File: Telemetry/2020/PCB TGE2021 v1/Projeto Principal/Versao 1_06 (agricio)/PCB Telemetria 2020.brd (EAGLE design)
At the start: 160 x 100 mm, 57 parts, among them IC1 INA240A1DR, IC2 MCP3221A6T-E_OTVAO, IC3 AZ1117IH-3.3TRG1, IC4 ACS758LCB-050B-PFF-T, IC5 ADS1115IDGSR, IC6 ACS712-030B3, IC7 THVD2410DR, J1 172042-0406, J2 39-28-9048, J3 39-28-9048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

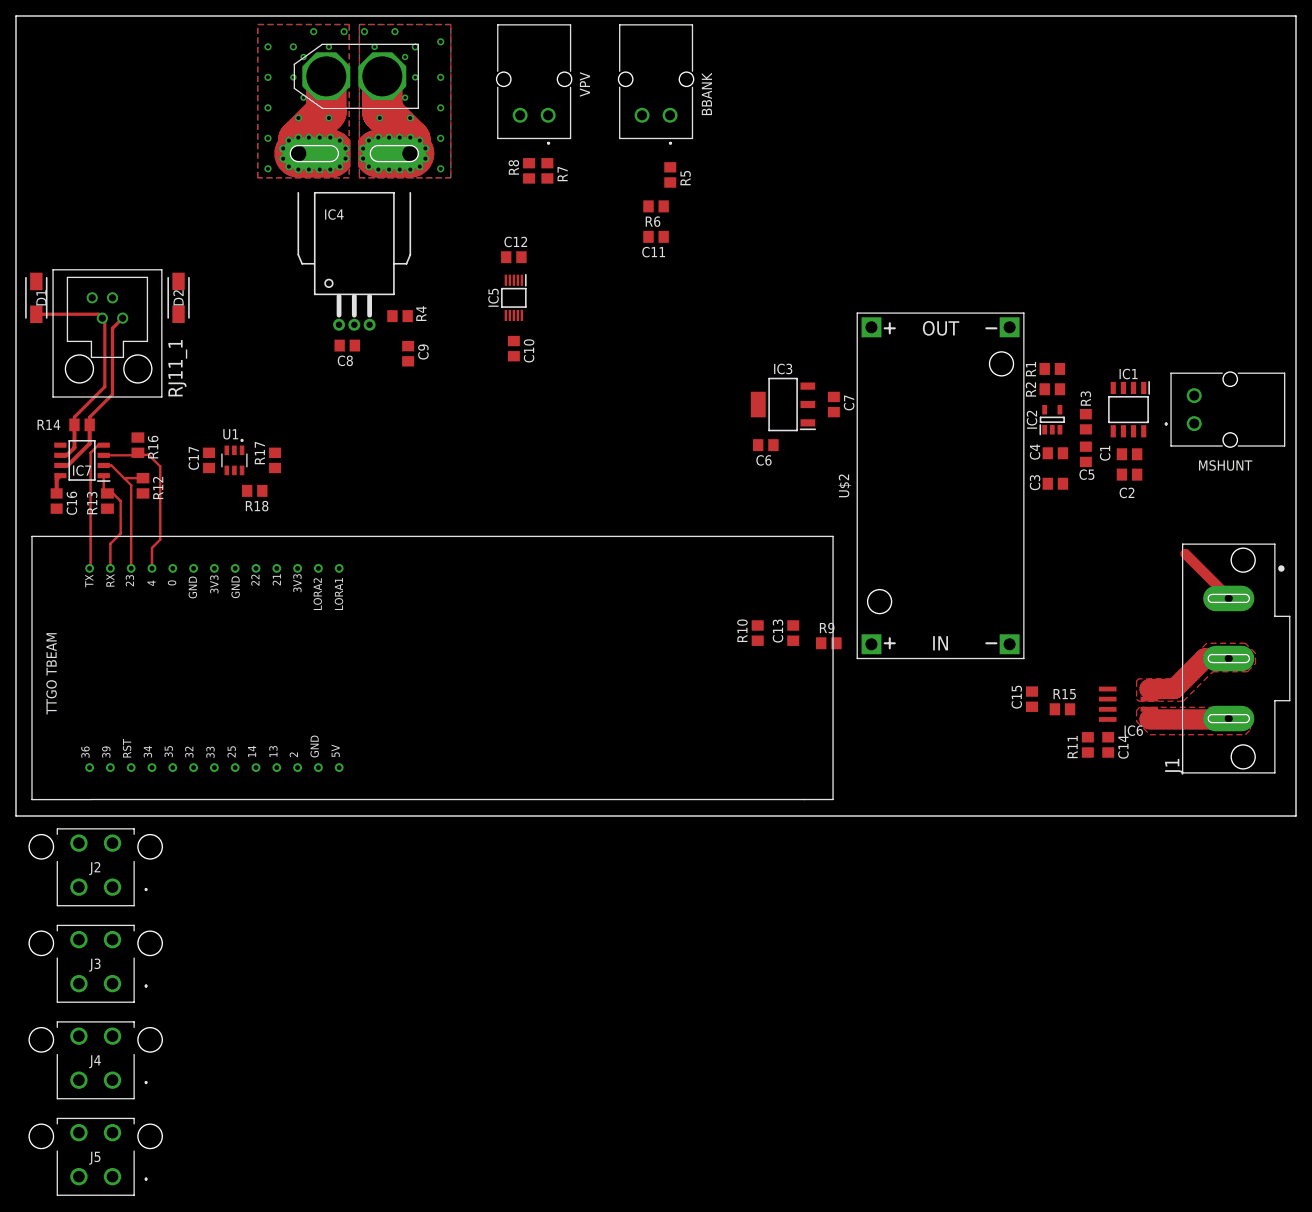
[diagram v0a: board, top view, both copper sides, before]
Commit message: Adicao do sensor de temperetura ao esquemático
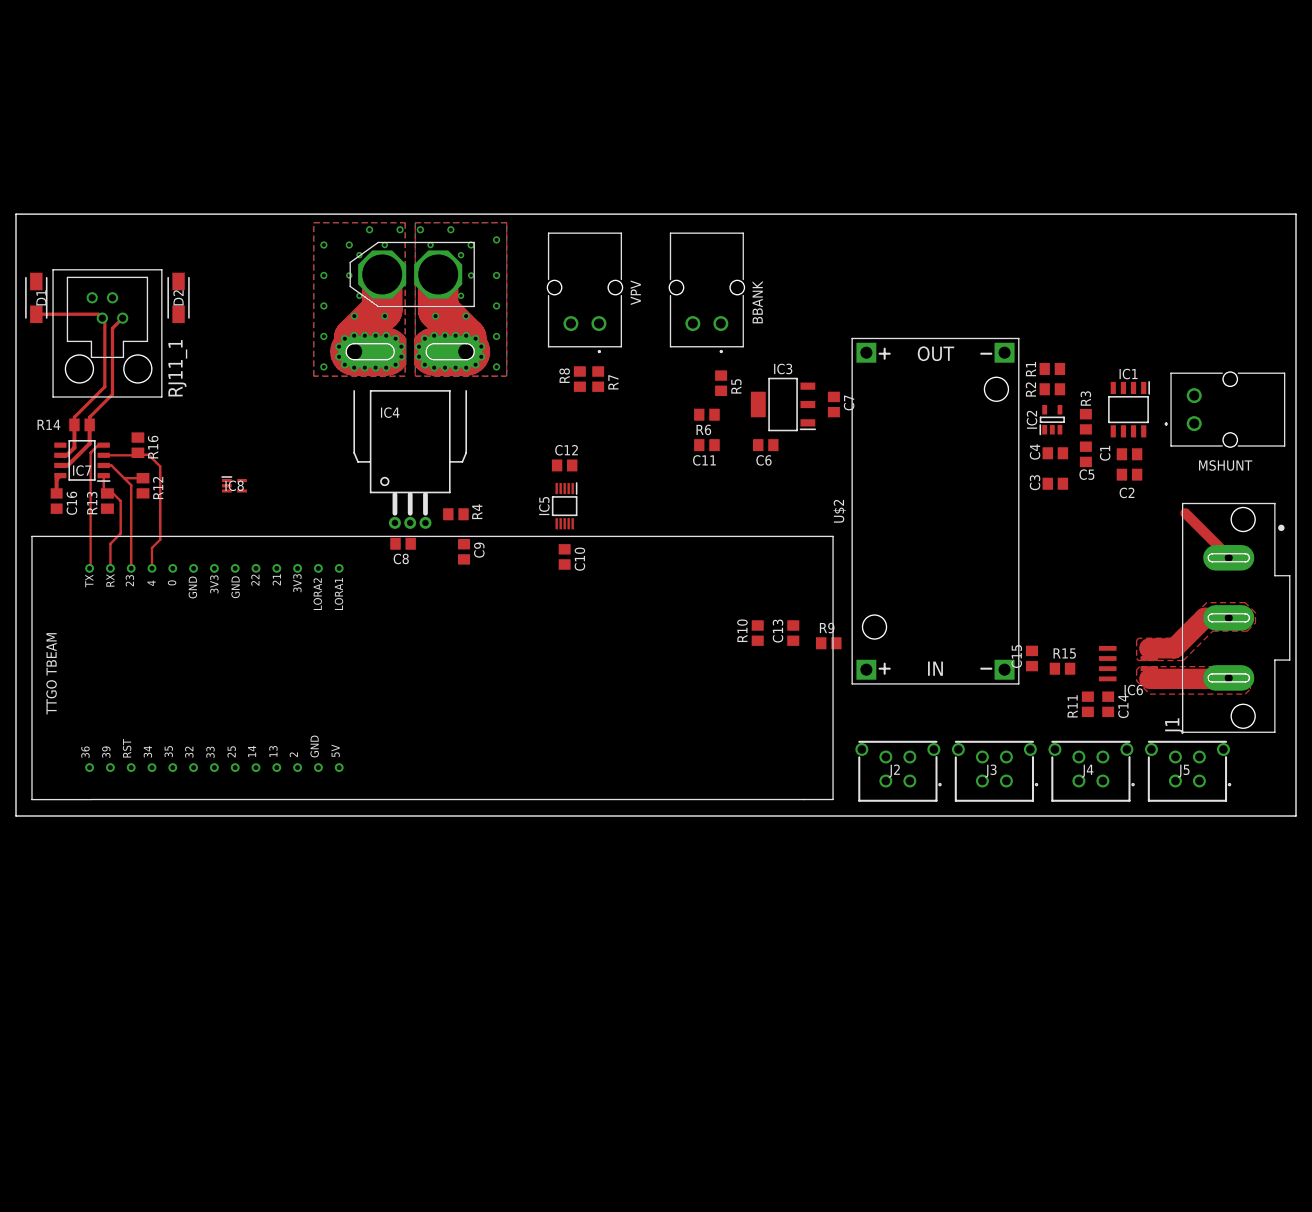
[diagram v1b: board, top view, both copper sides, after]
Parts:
- removed C17: 10nF, rcl:C0805
- removed R17, R18: 5k, rcl:R0805
- removed U1: TMP100NA/3K, TMP100NA_3K:SOT95P280X145-6N
- added IC8: TMP235AEDCKRQ1, SamacSys_Parts:SOT65P210X110-5N
- J2, J3, J4, J5: value 39-28-9048 -> 43045-0412; device SamacSys_Parts:39289048 -> SamacSys_Parts:43045-0412
- moved J5 137.8 mm to (141.6, 1.91)
- moved J4 122.6 mm to (129.5, 1.91)
- moved J3 107.9 mm to (117.5, 1.91)
- moved J2 94.0 mm to (105.4, 1.91)
- moved C10 26.8 mm to (68.6, 32.4)
- moved C11 26.8 mm to (86.4, 46.4)
- moved R5 26.8 mm to (88.1, 54.1)
- moved R6 26.8 mm to (86.4, 50.2)
- moved BBANK 26.8 mm to (86.4, 65.4)
- moved C12 26.8 mm to (68.6, 43.8)
- moved IC5 26.8 mm to (68.6, 38.7)
- moved R7 26.8 mm to (72.8, 54.6)
- moved R8 26.8 mm to (70.5, 54.6)
- moved VPV 26.8 mm to (71.1, 65.4)
- moved IC4 25.7 mm to (49.3, 58.0)
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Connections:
- net GND: no longer C17.2, U1.2, U1.3, U1.5
- net I2C_SCL: no longer R17.2, U1.1
- net I2C_SDA: no longer R18.1, U1.6
- net VCC_3V3: no longer C17.1, R17.1, R18.2, U1.4
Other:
- board size 160 x 100 mm -> 160 x 75.2 mm
